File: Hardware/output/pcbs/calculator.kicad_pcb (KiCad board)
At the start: 2 copper layers, 70.5 x 143 mm, 46 parts, among them J1 Sharp_LCD

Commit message: feat: update hardware design layout tools and expand calculator UI and testing frameworks
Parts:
- added FID1: Fiducial_1mm_Mask2mm, Fiducial:Fiducial_1mm_Mask2mm, F.Cu at (5.00, 140.0)
- added FID2: Fiducial_1mm_Mask2mm, Fiducial:Fiducial_1mm_Mask2mm, F.Cu at (60.0, 140.0)
- added FID3: Fiducial_1mm_Mask2mm, Fiducial:Fiducial_1mm_Mask2mm, F.Cu at (60.0, 20.0)
- added REF**: MountingHole_3.2mm_M3, MountingHole:MountingHole_3.2mm_M3, F.Cu at (18.9, -144.1)
- added REF**: MountingHole_3.2mm_M3, MountingHole:MountingHole_3.2mm_M3, F.Cu at (18.9, -16.9)
- added REF**: MountingHole_3.2mm_M3, MountingHole:MountingHole_3.2mm_M3, F.Cu at (71.6, -144.1)
- added REF**: MountingHole_3.2mm_M3, MountingHole:MountingHole_3.2mm_M3, F.Cu at (71.6, -16.9)
- B1, B10, B11, B12, B13, B14, B15, B16, B17, B18, B19, B2, B20, B21, B22, B23, B24, B25, B26, B27, B28, B29, B3, B30, B31, B32, B33, B34, B35, B36, B37, B4, B5, B6, B7, B8, B9: value (none) -> Tactile Switch 6x6mm
- J1: value Sharp_LCD -> Sharp_LCD_10Pin; footprint (none) -> Connector_FFC-FPC:Hirose_FH12-10S-0.5SH_1x10-1MP_P0.50mm_Horizontal
- JST1: value (none) -> JST-PH 2.0 2-Pin
- MCU1: value (none) -> RASPBERRY PI PICO
- moved JST1 131.0 mm to (68.0, -139.0)
- moved B1 6.00 mm to (23.0, -72.9)
- moved B10 6.00 mm to (50.5, -84.9)
- moved B11 6.00 mm to (50.5, -96.9)
- moved B12 6.00 mm to (61.5, -72.9)
- moved B13 6.00 mm to (61.5, -84.9)
- moved B14 6.00 mm to (61.5, -96.9)
- moved B15 6.00 mm to (72.5, -72.9)
- moved B16 6.00 mm to (72.5, -84.9)
- moved B17 6.00 mm to (72.5, -96.9)
- moved B2 6.00 mm to (17.5, -84.9)
- moved B3 6.00 mm to (17.5, -96.9)
- moved B4 6.00 mm to (28.5, -84.9)
- moved B5 6.00 mm to (28.5, -96.9)
- moved B6 6.00 mm to (39.5, -72.9)
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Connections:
- J1 pad 5: (no net) -> GND
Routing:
- net P21: track 193.7 -> 51.6 mm, vias 2 -> 0
- net VCC: track 157.3 -> 48.4 mm, vias 1 -> 0
- net GND: track 171.8 -> 67.0 mm, vias 1 -> 0
- net P20: track 86.5 -> 131.7 mm, vias 1 -> 3
- net P10: track 159.6 -> 195.4 mm, vias 2 -> 4
- net P15: track 177.1 -> 142.1 mm
- net P6: track 163.4 -> 197.1 mm, vias 2 -> 5
- net P1: track 135.5 -> 165.9 mm, vias 2 -> 4
- net P14: track 173.9 -> 153.6 mm
- net P8: track 164.3 -> 146.5 mm
- net P5: track 150.8 -> 167.1 mm, vias 2 -> 4
- net P18: track 5.74 -> 19.9 mm, vias 1 -> 0
- net P0: track 128.9 -> 141.5 mm, vias 2 -> 6
- net P4: track 143.5 -> 132.8 mm, vias 1 -> 4
- net P16: track 94.4 -> 103.8 mm
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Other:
- board size 70.5 x 143 mm -> 66.7 x 141.7 mm
- board text added: "WatchCalc 32"

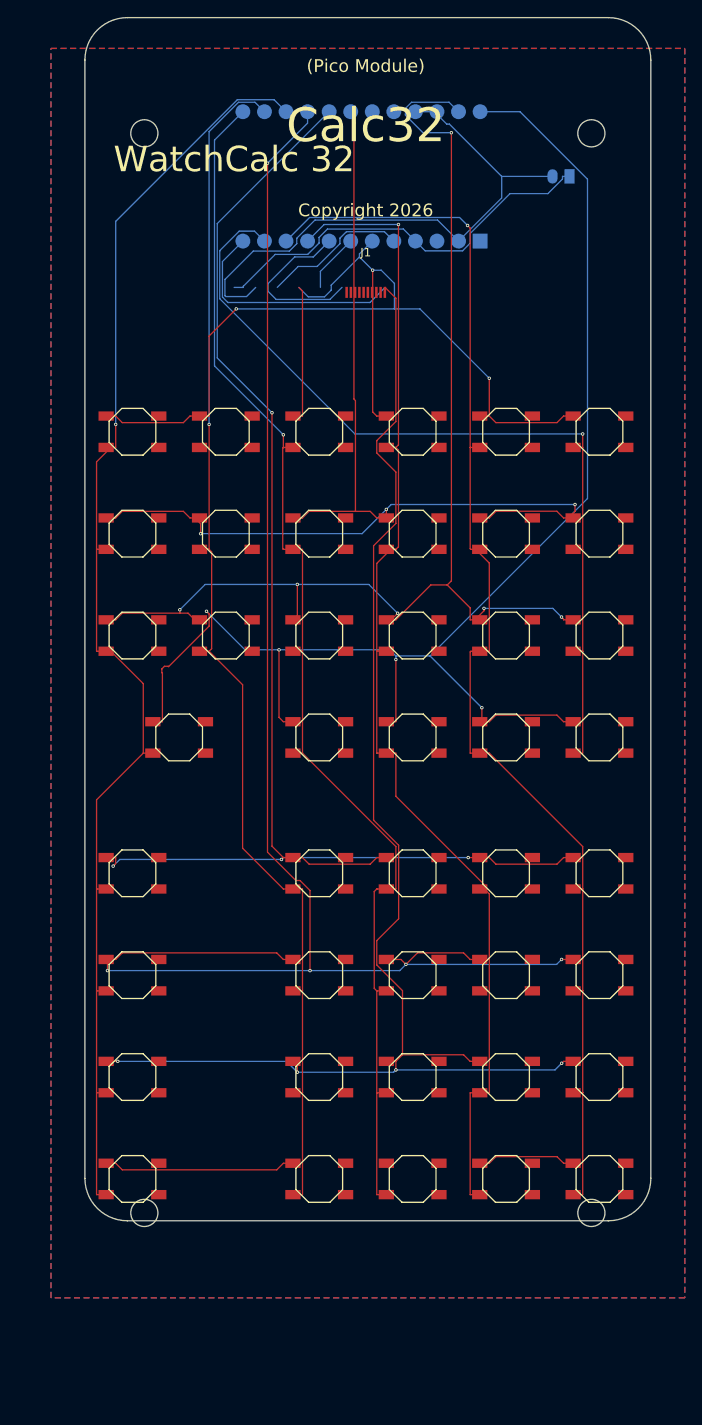
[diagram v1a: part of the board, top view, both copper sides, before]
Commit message: refactor: reorganize hardware manufacturing files, remove legacy build outputs, and update project structure for firmware and UI components.
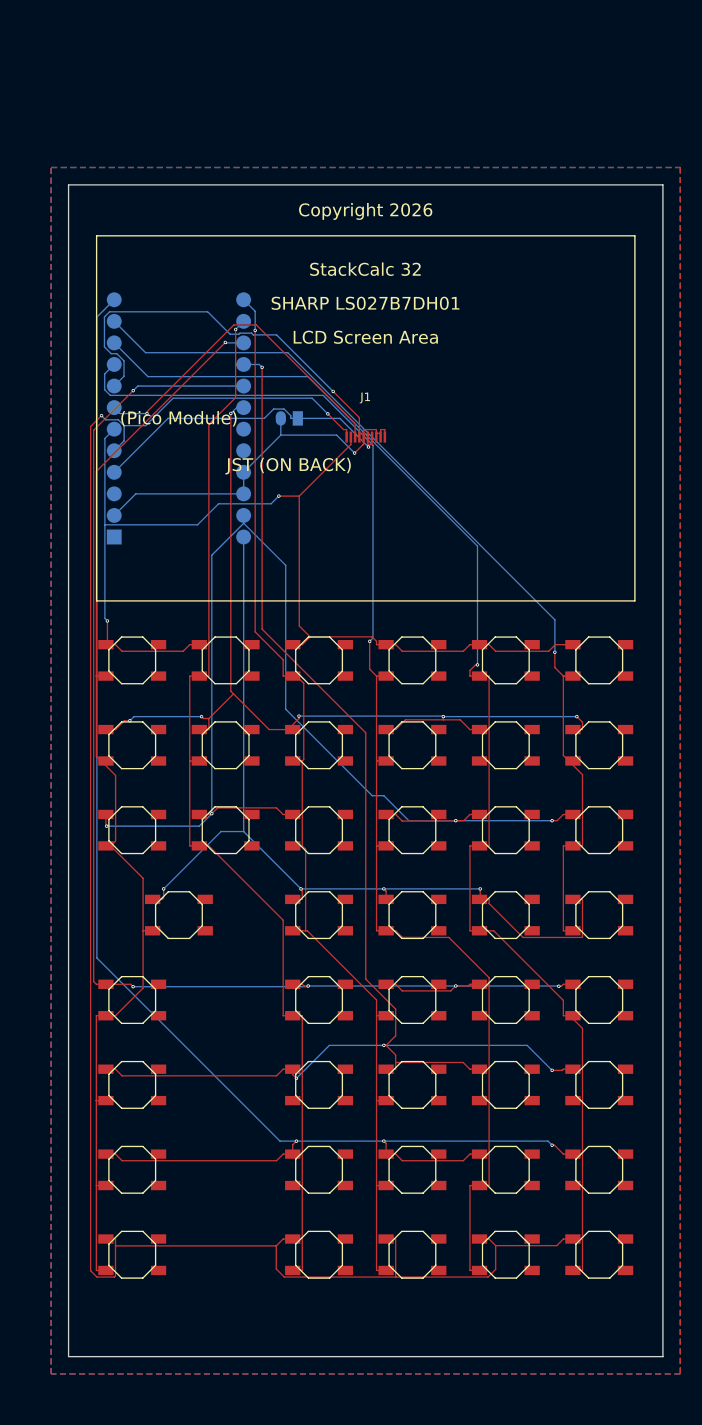
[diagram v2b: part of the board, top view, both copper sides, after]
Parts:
- removed REF** (x4): MountingHole_3.2mm_M3, MountingHole:MountingHole_3.2mm_M3
- moved JST1 42.9 mm to (36.0, -110.5)
- moved MCU1 35.7 mm to (23.0, -110.5), turned to 90 degrees
- moved SOFT1 26.9 mm to (17.5, -82.0)
- moved SOFT2 26.9 mm to (28.5, -82.0)
- moved SOFT3 26.9 mm to (39.5, -82.0)
- moved SOFT4 26.9 mm to (50.5, -82.0)
- moved SOFT5 26.9 mm to (61.5, -82.0)
- moved SOFT6 26.9 mm to (72.5, -82.0)
- moved B11 24.9 mm to (50.5, -72.0)
- moved B14 24.9 mm to (61.5, -72.0)
- moved B17 24.9 mm to (72.5, -72.0)
- moved B3 24.9 mm to (17.5, -72.0)
- moved B5 24.9 mm to (28.5, -72.0)
- moved B8 24.9 mm to (39.5, -72.0)
- moved B10 22.9 mm to (50.5, -62.0)
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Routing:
- net P21: track 51.6 -> 217.1 mm, vias 0 -> 2
- net P1: track 165.9 -> 105.0 mm
- net P6: track 197.1 -> 163.4 mm, vias 5 -> 4
- net P19: track 6.93 -> 39.5 mm, vias 0 -> 1
- net P18: track 19.9 -> 47.8 mm, vias 0 -> 1
- net P7: track 155.3 -> 130.9 mm
- net GND: track 67.0 -> 44.9 mm, vias 0 -> 1
- net P4: track 132.8 -> 113.2 mm, vias 4 -> 6
- net P9: track 148.4 -> 130.3 mm
- net P8: track 146.5 -> 128.4 mm
- net P10: track 195.4 -> 181.6 mm, vias 4 -> 3
- net P15: track 142.1 -> 154.5 mm
- net P5: track 167.1 -> 155.1 mm, vias 4 -> 5
- net VCC: track 48.4 -> 37.6 mm, vias 0 -> 1
- net P20: track 131.7 -> 123.8 mm, vias 3 -> 2
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- added copper zone on B.Cu, net (none)
- added copper zone on F.Cu, net (none)
- removed copper zone on B.Cu, net GND
- removed copper zone on F.Cu, net GND
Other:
- board size 66.7 x 141.7 mm -> 70 x 138 mm
- board text added: "JST (ON BACK)"
- board text added: "LCD Screen Area"
- board text added: "SHARP LS027B7DH01"
- board text added: "StackCalc 32"
- board text removed: "Calc32"
- board text removed: "WatchCalc 32"

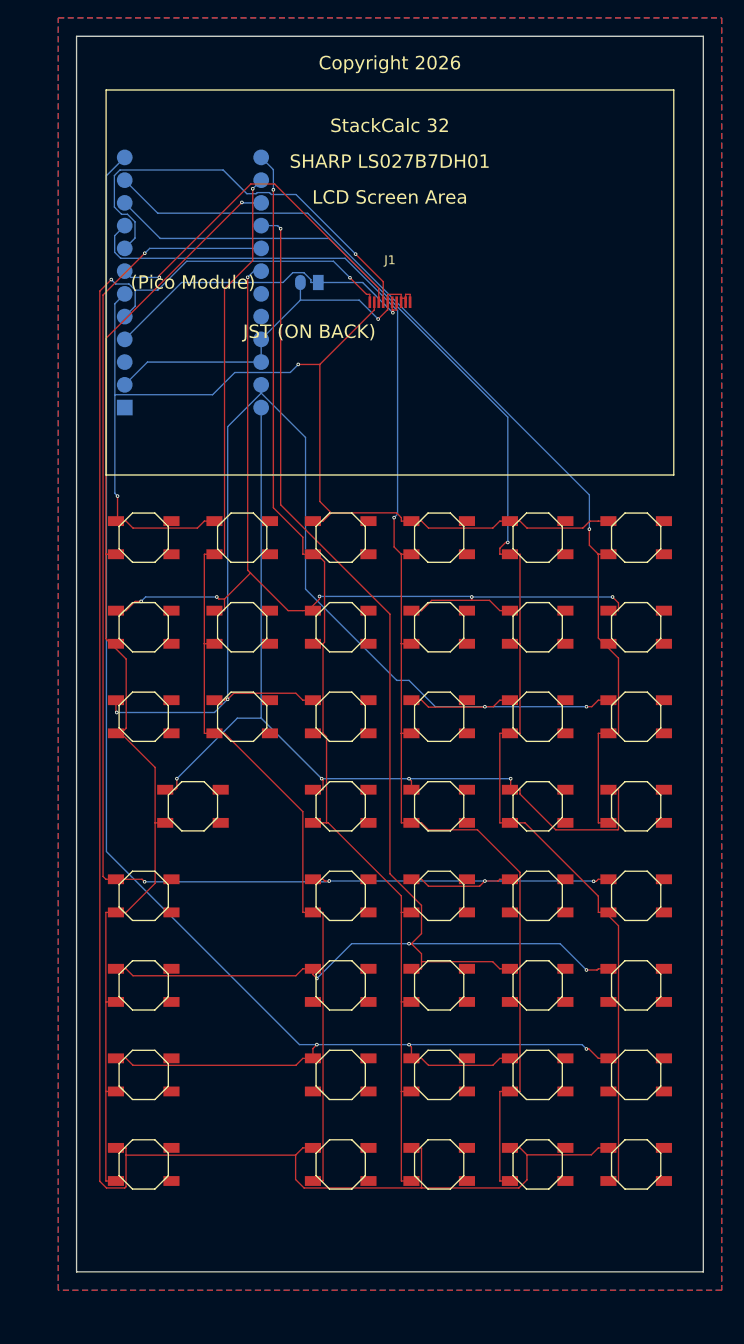
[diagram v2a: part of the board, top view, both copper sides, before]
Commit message: refactor: remove tactile switches from PCB and update hardware manufacturing and UI scripts
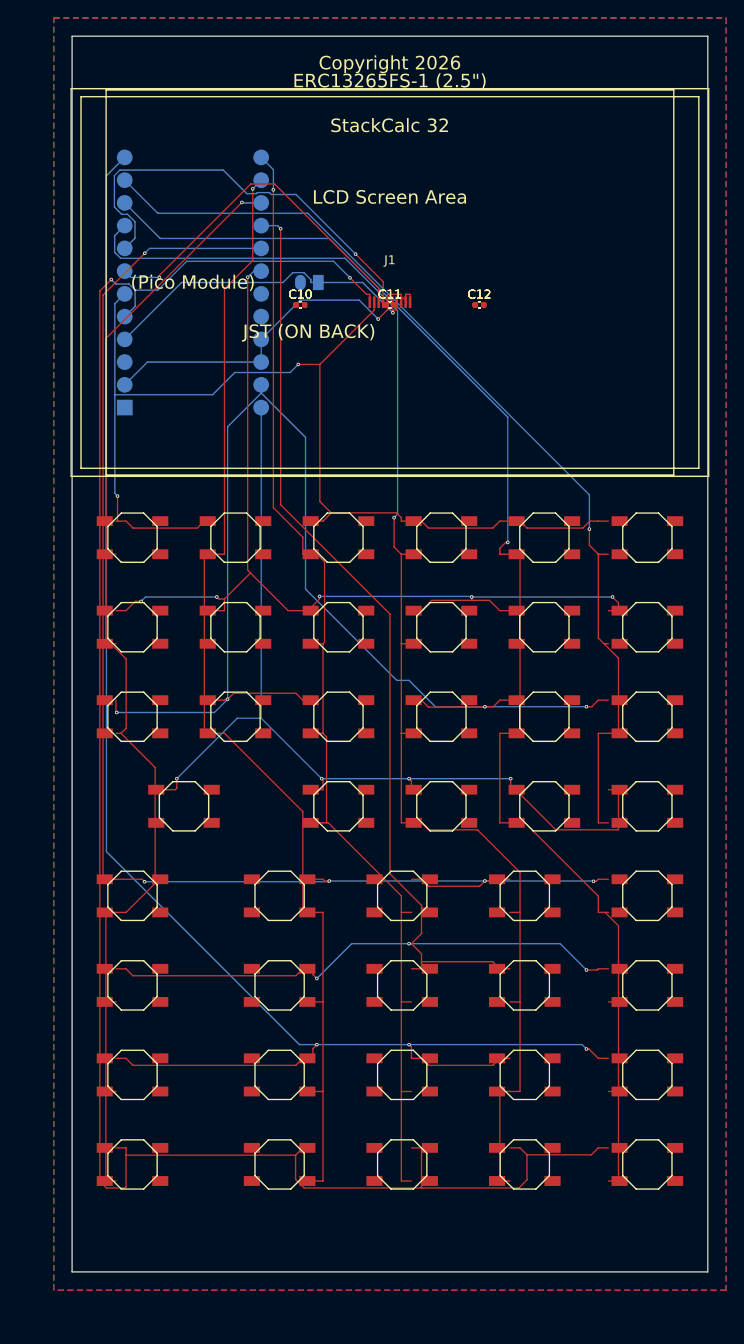
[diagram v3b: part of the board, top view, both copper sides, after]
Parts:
- added C10 (x3): C_0402_1005Metric, C_0402_1005Metric, F.Cu at (35.0, -108.0)
- added C11 (x3): C_0402_1005Metric, C_0402_1005Metric, F.Cu at (45.0, -108.0)
- added C12 (x3): C_0402_1005Metric, C_0402_1005Metric, F.Cu at (55.0, -108.0)
- moved B22 6.82 mm to (32.7, -42.0)
- moved B23 6.82 mm to (32.7, -32.0)
- moved B24 6.82 mm to (32.7, -22.0)
- moved B25 6.82 mm to (32.7, -12.0)
- moved B26 4.13 mm to (46.4, -42.0)
- moved B27 4.13 mm to (46.4, -32.0)
- moved B28 4.13 mm to (46.4, -22.0)
- moved B29 4.13 mm to (46.4, -12.0)
- moved B30 1.44 mm to (60.1, -42.0)
- moved B31 1.44 mm to (60.1, -32.0)
- moved B32 1.44 mm to (60.1, -22.0)
- moved B33 1.44 mm to (60.1, -12.0)
- moved B15 1.25 mm to (73.8, -52.0)
- moved B16 1.25 mm to (73.8, -62.0)
- moved B17 1.25 mm to (73.8, -72.0)
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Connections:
- J1 pad 1: P21 -> Net-(J1-Pad1)
- J1 pad 10: GND -> Net-(J1-Pad10)
- J1 pad 2: P20 -> Net-(J1-Pad2)
- J1 pad 3: P19 -> Net-(J1-Pad3)
- J1 pad 4: P18 -> Net-(J1-Pad4)
- J1 pad 5: GND -> Net-(J1-Pad5)
- J1 pad 6: VCC -> +3V3
- J1 pad 7: VCC -> GND
- J1 pad 8: GND -> Net-(J1-Pad8)
- J1 pad 9: GND -> Net-(J1-Pad9)
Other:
- board size 70 x 138 mm -> 71 x 138 mm
- board text added: "Active Area"
- board text added: "Boss L"
- board text added: "Boss R"
- board text added: "CR2032 Bucket"
- board text added: "Chassis Cavity"
- board text added: "ERC13265FS-1 (2.5")"
- board text added: "LCD Glass"
- board text removed: "SHARP LS027B7DH01"

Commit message: refactor: update PCB component layout and add peripheral utility scripts for hardware maintenance
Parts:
- removed C10 (x3), C11 (x3), C12 (x3): C_0402_1005Metric, C_0402_1005Metric
- removed FID1, FID2, FID3: Fiducial_1mm_Mask2mm, Fiducial:Fiducial_1mm_Mask2mm
- added C1: , , F.Cu at (35.0, -106.0)
- added C2: , , F.Cu at (37.5, -106.0)
- added C3: , , F.Cu at (40.0, -106.0)
- added C4: , , F.Cu at (42.5, -106.0)
- added C5: , , F.Cu at (45.0, -106.0)
- added C6: , , F.Cu at (47.5, -106.0)
- added C7: , , F.Cu at (50.0, -106.0)
- added C8: , , F.Cu at (52.5, -106.0)
- B1, B10, B11, B12, B13, B14, B15, B16, B17, B18, B19, B2, B20, B21, B22, B23, B24, B25, B26, B27, B28, B29, B3, B30, B31, B32, B33, B34, B35, B36, B37, B4, B5, B6, B7, B8, B9: value Tactile Switch 6x6mm -> (none)
- J1: value Sharp_LCD_10Pin -> Sharp_LCD; footprint Connector_FFC-FPC:Hirose_FH12-10S-0.5SH_1x10-1MP_P0.50mm_Horizontal -> (none)
- JST1: value JST-PH 2.0 2-Pin -> (none)
- MCU1: value RASPBERRY PI PICO -> (none)
- moved JST1 44.7 mm to (71.9, -137.1), turned to 0 degrees
- moved MCU1 25.4 mm to (47.2, -103.0)
- moved SOFT1 21.0 mm to (17.5, -102.9)
- moved SOFT6 21.0 mm to (72.5, -102.9)
- moved SOFT2 20.9 mm to (28.5, -102.9)
- moved SOFT5 20.9 mm to (61.5, -102.9)
- moved SOFT3 20.9 mm to (39.5, -102.9)
- moved SOFT4 20.9 mm to (50.5, -102.9)
- moved B3 19.0 mm to (17.5, -90.9)
- moved B17 19.0 mm to (72.5, -90.9)
- moved B5 18.9 mm to (28.5, -90.9)
- moved B14 18.9 mm to (61.5, -90.9)
- moved B8 18.9 mm to (39.5, -90.9)
- moved B11 18.9 mm to (50.5, -90.9)
- moved B2 17.0 mm to (17.5, -78.9)
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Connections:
- J1 pad 1: Net-(J1-Pad1) -> (no net)
- J1 pad 10: Net-(J1-Pad10) -> (no net)
- J1 pad 5: Net-(J1-Pad5) -> GND
- J1 pad 6: +3V3 -> GND
- J1 pad 7: GND -> (no net)
- J1 pad 8: Net-(J1-Pad8) -> (no net)
- J1 pad 9: Net-(J1-Pad9) -> (no net)
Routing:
- net P21: track 217.1 -> 157.6 mm, vias 2 -> 1
- net P0: track 137.9 -> 89.3 mm
- net P20: track 123.8 -> 75.2 mm, vias 2 -> 1
- net P18: track 47.8 -> 0.00 mm, vias 1 -> 0
- net GND: track 44.9 -> 92.3 mm
- net P19: track 39.5 -> 0.00 mm, vias 1 -> 0
- net P5: track 155.1 -> 125.4 mm, vias 5 -> 4
- net P14: track 155.5 -> 127.0 mm
- net P15: track 154.5 -> 130.9 mm
- net P10: track 181.6 -> 162.1 mm, vias 3 -> 5
- net P6: track 163.4 -> 144.0 mm
- net P16: track 109.4 -> 92.2 mm
- net VCC: track 37.6 -> 54.6 mm, vias 1 -> 0
- net P4: track 113.2 -> 100.3 mm, vias 6 -> 4
- net P7: track 130.9 -> 142.6 mm
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- added copper zone on B.Cu, net GND
- added copper zone on F.Cu, net GND
- removed copper zone on B.Cu, net (none)
- removed copper zone on F.Cu, net (none)
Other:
- board size 71 x 138 mm -> 70.5 x 143 mm
- board text added: "Calc32"
- board text removed: "Active Area"
- board text removed: "Boss L"
- board text removed: "Boss R"
- board text removed: "CR2032 Bucket"
- board text removed: "Chassis Cavity"
- board text removed: "ERC13265FS-1 (2.5")"
- board text removed: "JST (ON BACK)"
- board text removed: "LCD Glass"
- board text removed: "LCD Screen Area"
- board text removed: "StackCalc 32"
